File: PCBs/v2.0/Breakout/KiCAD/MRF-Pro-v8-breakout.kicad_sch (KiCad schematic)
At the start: 6 parts, among them J5 FPC 8P Connector, J6 Stemma QT, J7 TFS20L / DTS6012M

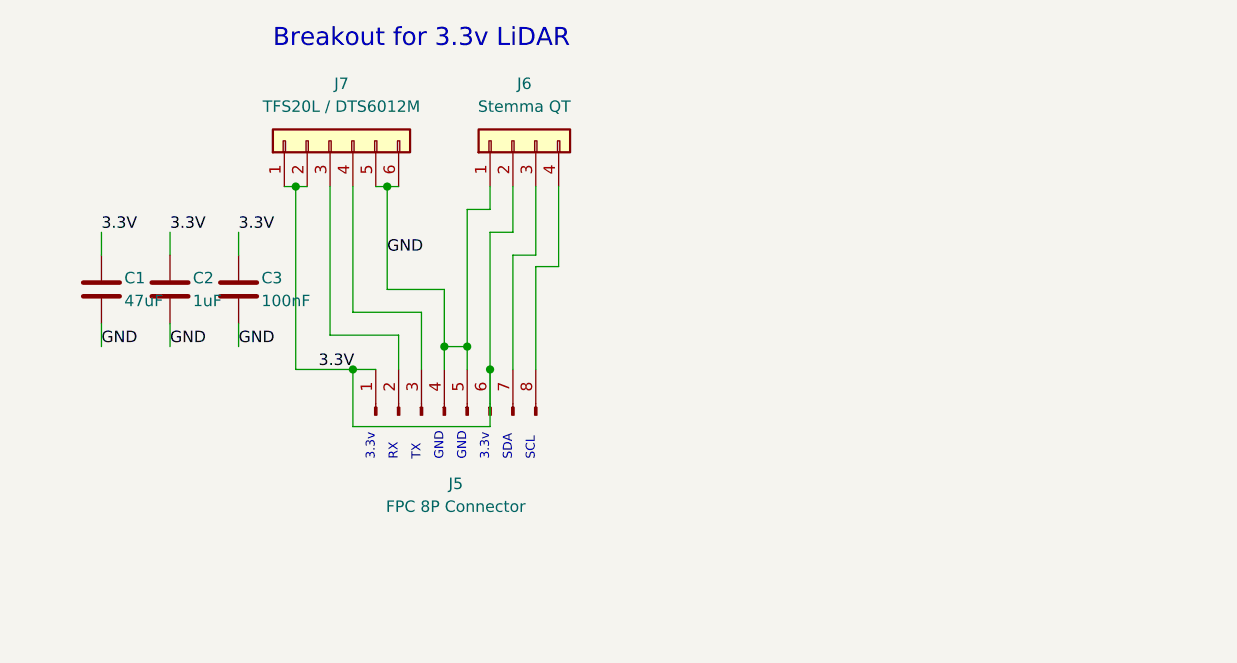
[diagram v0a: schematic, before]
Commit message: Capture dedicated LiDAR LDO in the breakout and main schematics
Breakout (MRF-Pro-v8-breakout): add U1 TLV75533 3.3V LDO with input
decoupling (Cin1 1uF, Cin2 10uF) and FB1 (0R default) splitting the
regulator output net 3V3_LIDAR from the laser bulk net 3V3_LASER.
J7 pin1 moves to 3V3_LASER (with the 47uF C1), pin2 to 3V3_LIDAR (with
C2/C3 at U1 OUT); J5 pin6 becomes VBAT feeding U1 IN; U1 EN sits on the
FPC pin1 net and U1 pin4 (NC) is flagged no-connect. C1/C2/C3 reused as
the output network. ERC clean, 0 warnings.

Main (MRF-Pro-v8): wire the Feather BAT pin (J2 pin12) to a new VBAT net
through to FPC pin6, detaching pin6 from its old J4-pin8 net and
no-connecting the freed J4 pin8. 3.3V rail unchanged. ERC: 0 errors
(one pre-existing dangling-wire warning unchanged).

Schematic capture and ERC/netlist verification only; PCB layout to follow.
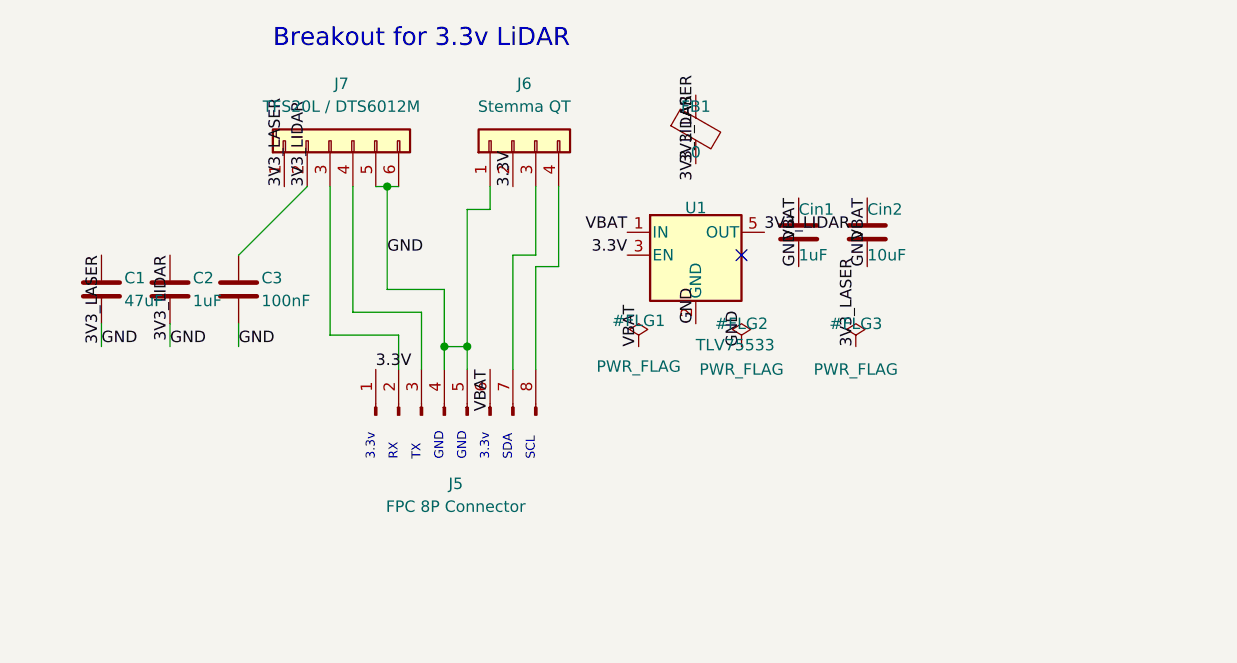
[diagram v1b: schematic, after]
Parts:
- added Cin1: 1uF, Capacitor_SMD:C_0402_1005Metric, symbol Device:C
- added Cin2: 10uF, Capacitor_SMD:C_0805_2012Metric, symbol Device:C
- added FB1: 0, Inductor_SMD:L_0805_2012Metric, symbol Device:FerriteBead
- added U1: TLV75533, Package_TO_SOT_SMD:SOT-23-5, symbol Regulator_Linear:TLV75533PDBV
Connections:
- net 3.3V: now also U1.3 (EN); no longer C1.1, C2.1, C3.1, J5.6 (Pin_6), J7.1 (Pin_1), J7.2 (Pin_2)
- net GND: now also Cin1.2, Cin2.2, U1.2 (GND)
- new net 3V3_LASER: C1.1, FB1.2, J7.1 (Pin_1)
- new net 3V3_LIDAR: C2.1, C3.1, FB1.1, J7.2 (Pin_2), U1.5 (OUT)
- new net VBAT: Cin1.1, Cin2.1, J5.6 (Pin_6), U1.1 (IN)
- no-connect marks 0 -> 1

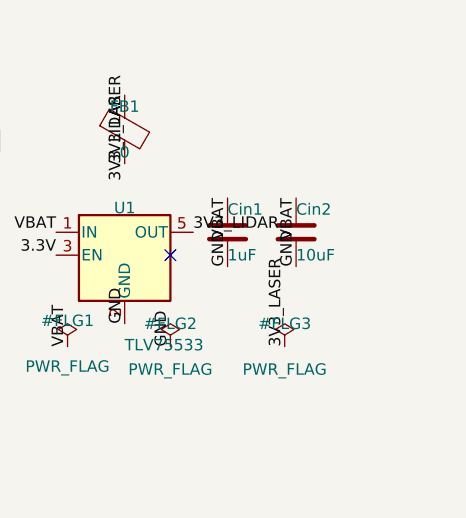
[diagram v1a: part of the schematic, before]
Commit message: Add the LiDAR LDO EN pulldown and source the breakout BOM
R1 (100k) holds the TLV75533 enable low at power-off. The part has no
internal EN pulldown, so the switched 3.3V rail on FPC pin 1 alone
would not guarantee the regulator shuts down; R1 gives EN a defined
path to ground. Placed and routed next to U1, clear of the laser-pulse
and output-cap clusters. DRC clean.

Add LCSC part numbers (U1, Cin1, Cin2, FB1, R1) for the JLCPCB
assembly BOM.
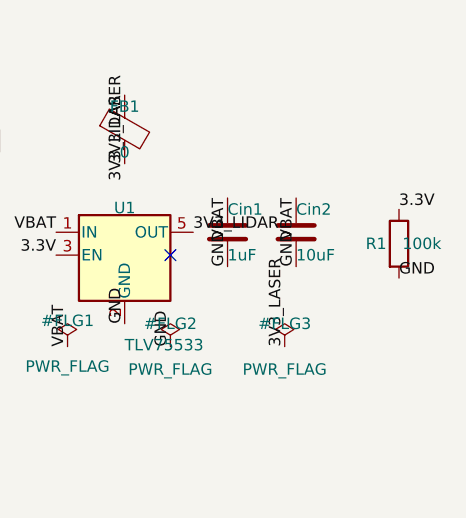
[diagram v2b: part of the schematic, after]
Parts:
- added R1: 100k, Resistor_SMD:R_0402_1005Metric, symbol Device:R
- Cin1: LCSC (none) -> C52923
- Cin2: LCSC (none) -> C15850
- FB1: LCSC (none) -> C2889442
- U1: LCSC (none) -> C404027
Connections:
- net 3.3V: now also R1.1
- net GND: now also R1.2

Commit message: Complete the breakout assembly BOM (C1, C2, C3, J6 LCSC)
Add LCSC numbers for the last unsourced assembled parts: C1 47uF 1206
(C96123), C2 1uF 0603 (C15849), C3 100nF 0402 (C1525), J6 Stemma QT
JST-SH (C160404). J7 (the DTS6012M module) plugs in and is the only
part left off the assembly BOM by design.
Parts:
- C1: LCSC (none) -> C96123
- C2: LCSC (none) -> C15849
- C3: LCSC (none) -> C1525
- J6: LCSC (none) -> C160404

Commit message: Source the J7 LiDAR connector (LCSC C160405)
J7 is the board-side JST-SH SM06B-SRSS-TB 6-pin socket the DTS6012M
plugs into (not the module itself), so it is an assembled part. Add
its LCSC to complete the breakout assembly BOM.
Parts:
- J7: LCSC (none) -> C160405
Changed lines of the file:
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@@
 			)
 		)
+    (property "LCSC" "C160405" (at 139.7 77.47 0)
+      (effects (font (size 1.27 1.27)) (hide yes))
+    )
 		(pin "1"
 		)

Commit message: Switch connectors to in-stock parts and fix the 0-ohm jumper
Align the JST-SH connectors to the established v1/README parts instead
of genuine-JST Extended ones: J4 8-pin C7430450 (the main-board J4 had
a 6-pin number, C7430448, by mistake), J7 6-pin C7430448, J6 4-pin
C7430446. Swap FB1 to C17477 - the prior C2889442 was out of stock and
Extended; C17477 is Basic and well-stocked. Applied across schematic,
footprint fields, and the JLCPCB BOM on both boards.
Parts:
- FB1: LCSC C2889442 -> C17477
- J6: LCSC C160404 -> C7430446
- J7: LCSC C160405 -> C7430448
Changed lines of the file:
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@@
 			)
 		)
-		(property "LCSC" "C2889442"
+		(property "LCSC" "C17477"
 			(at 180.34 76.2 0)
 			(hide yes)
@@
 			)
 		)
-    (property "LCSC" "C160404" (at 160.02 77.47 0)
+    (property "LCSC" "C7430446" (at 160.02 77.47 0)
       (effects (font (size 1.27 1.27)) (hide yes))
     )
@@
 			)
 		)
-    (property "LCSC" "C160405" (at 139.7 77.47 0)
+    (property "LCSC" "C7430448" (at 139.7 77.47 0)
       (effects (font (size 1.27 1.27)) (hide yes))
     )

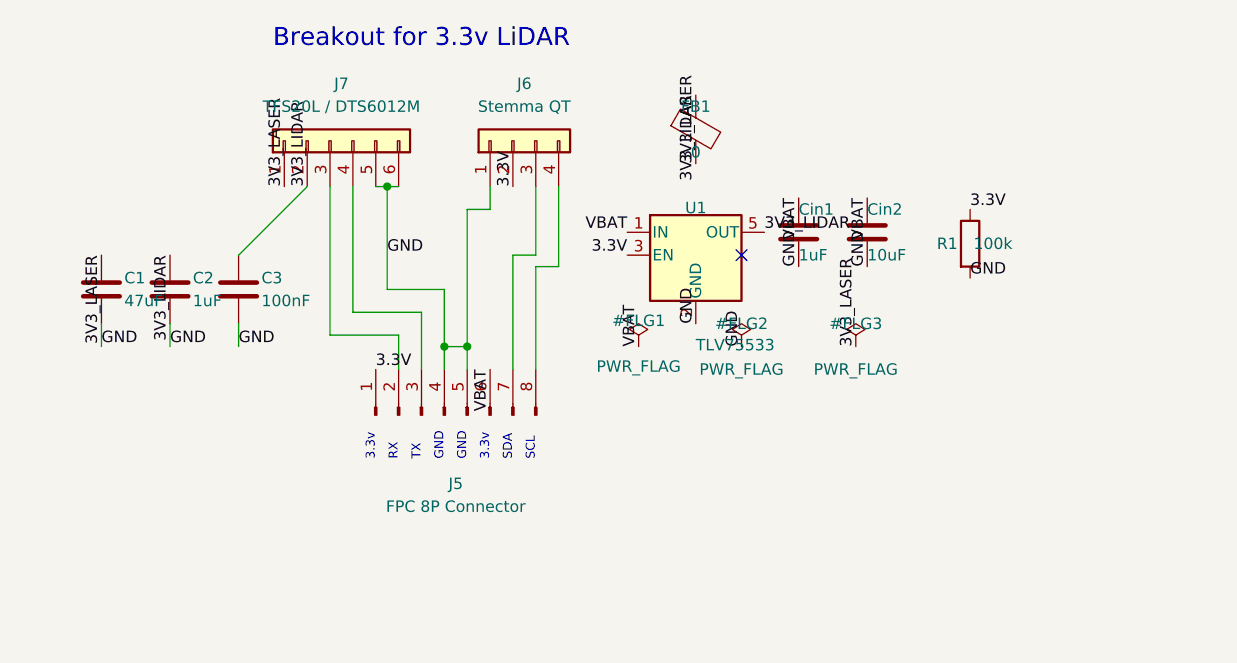
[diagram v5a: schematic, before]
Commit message: Swap FPC pins 1 and 6, reroute both boards, re-plot fab
VBAT now lands on FPC pin 1 (beside the UART pair) and the switched 3.3 V
on pin 6 (beside the I2C pair), so the always-on battery rail no longer
runs next to the I2C lines. Both boards' schematics were tidied up and
fully rerouted; DRC passes clean on each. Gerbers and the JLCPCB position
files are re-plotted to match. The BOM is unchanged - this is a net and
placement change, not a parts change.
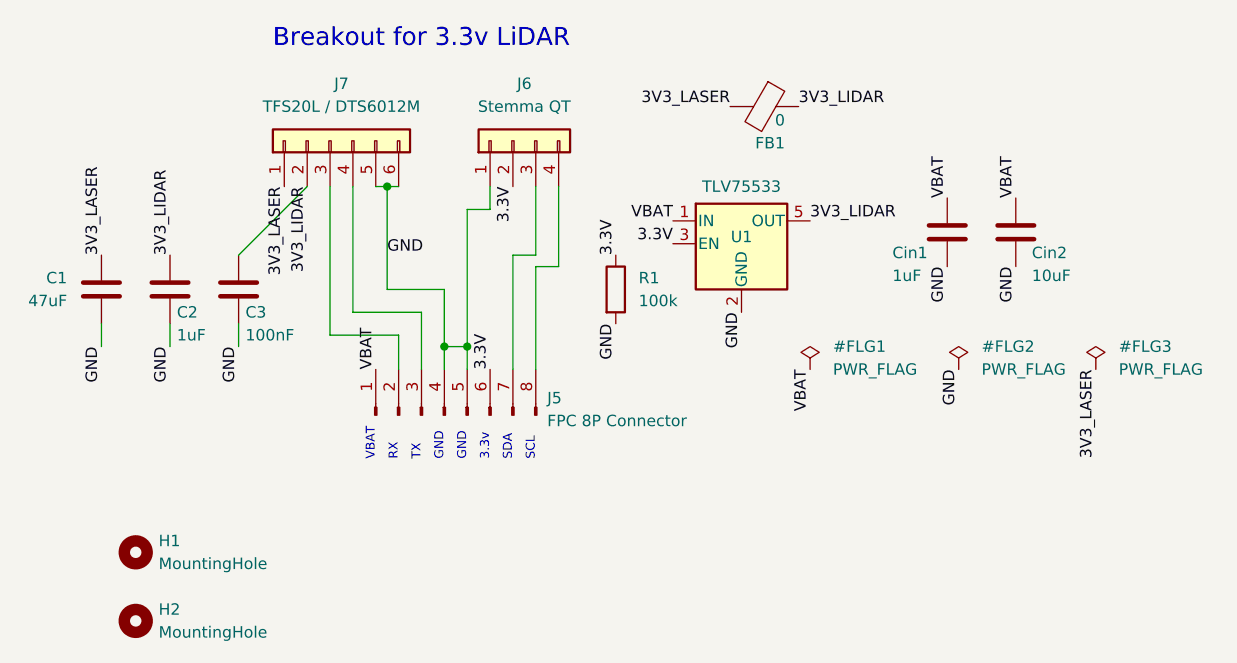
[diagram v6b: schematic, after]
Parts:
- added H1, H2: MountingHole, MountingHole:MountingHole_2.2mm_M2, symbol Mechanical:MountingHole
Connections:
- net 3.3V: now also J5.6 (Pin_6); no longer J5.1 (Pin_1)
- net VBAT: now also J5.1 (Pin_1); no longer J5.6 (Pin_6)
- no-connect marks 1 -> 0
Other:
- note added: "VBAT"
- moved on the sheet: Cin1, Cin2, FB1, R1, U1
